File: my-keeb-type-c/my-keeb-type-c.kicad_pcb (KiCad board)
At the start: 2 copper layers, 190.5 x 95.2 mm, 108 parts, among them SW1 SW_Push, U1 ATmega32U4-AU, Y1 16MHz

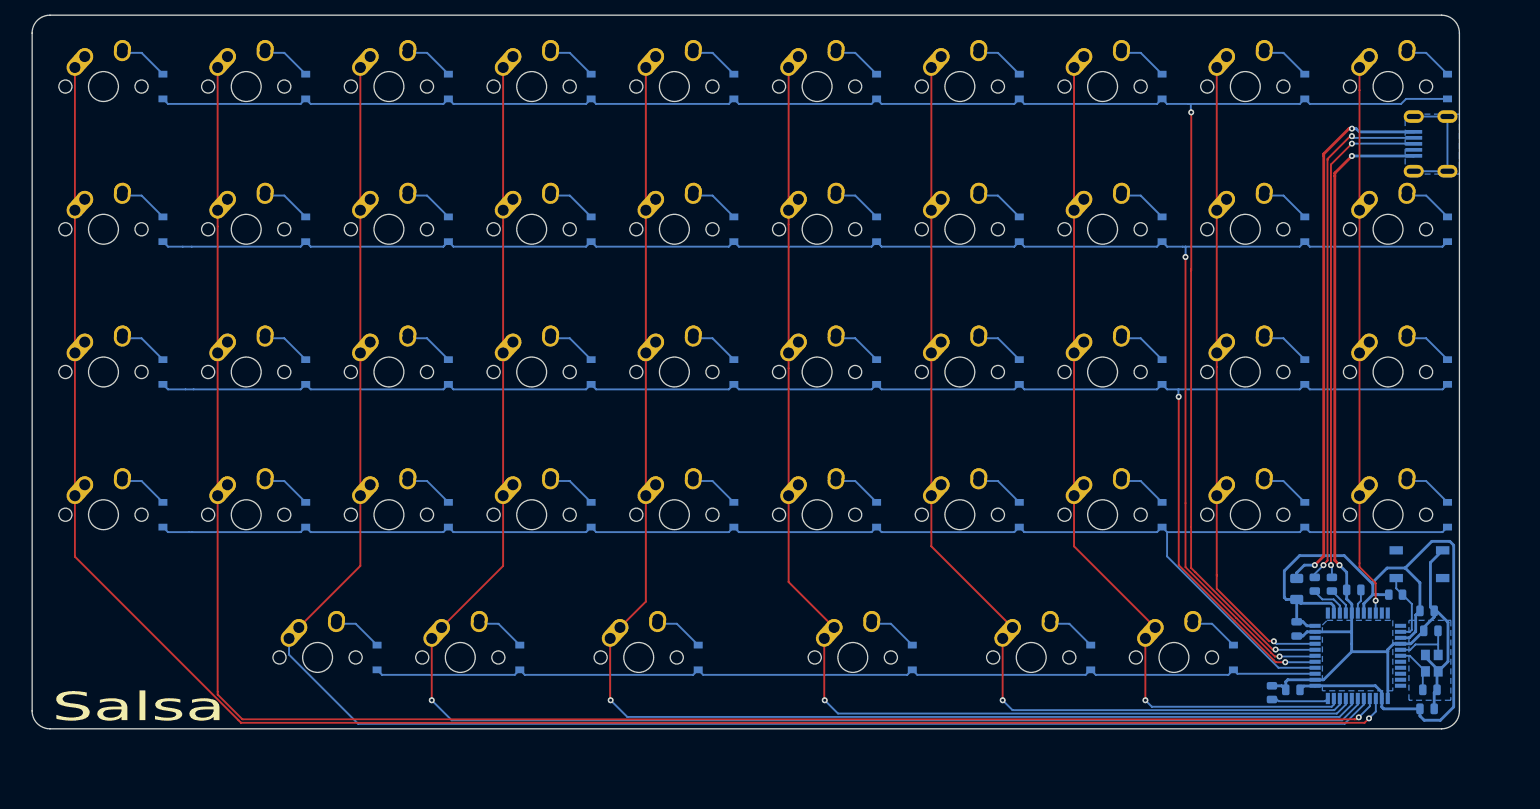
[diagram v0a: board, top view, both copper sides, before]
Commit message: Finished type c model
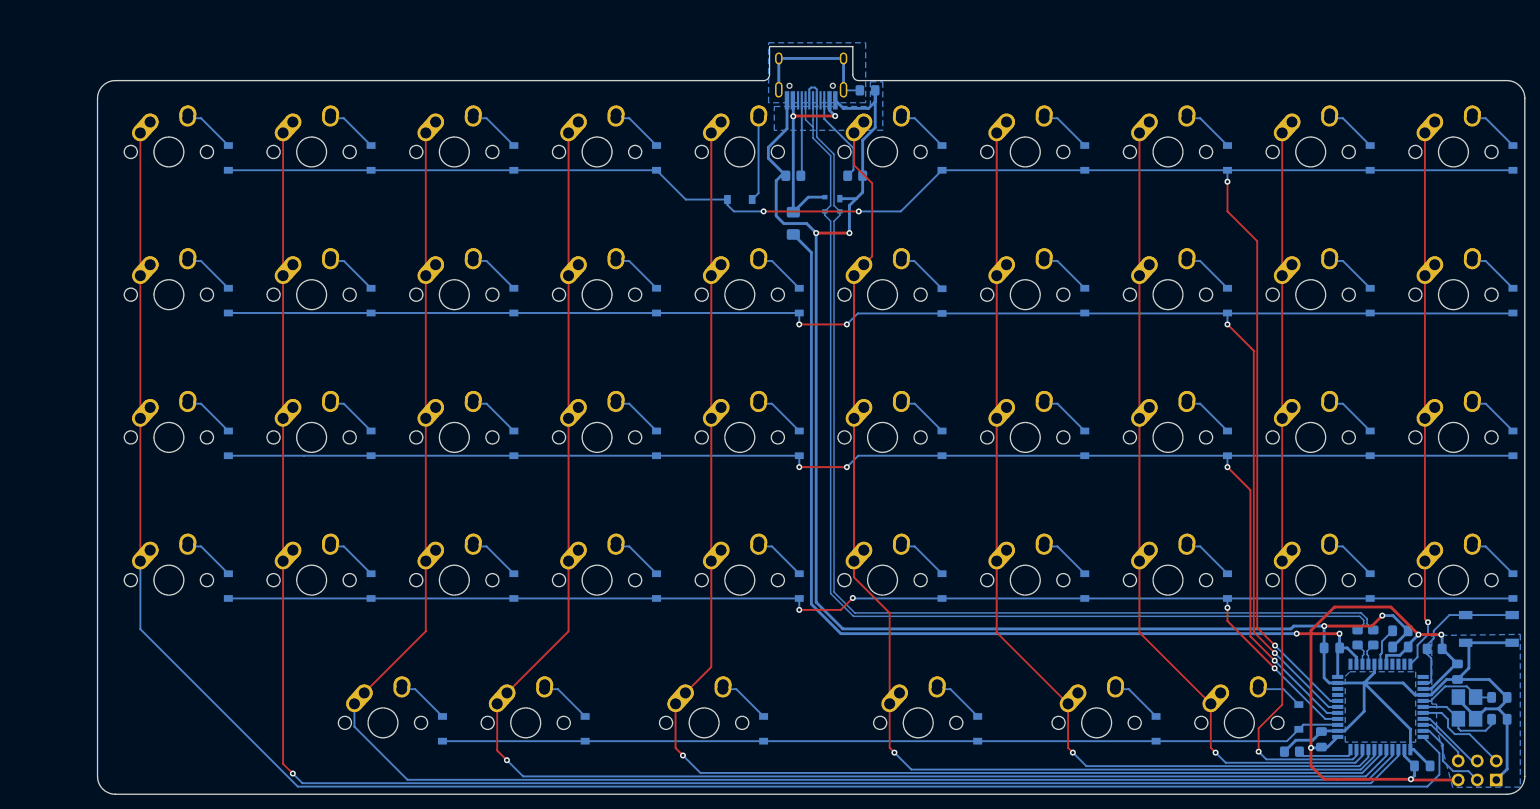
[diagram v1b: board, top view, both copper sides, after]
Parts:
- added C8: 10uF, Capacitor_SMD:C_0805_2012Metric_Pad1.18x1.45mm_HandSolder, B.Cu at (186.2, 97.2)
- added FB1: 60@100MHz, Inductor_SMD:L_0805_2012Metric_Pad1.15x1.40mm_HandSolder, B.Cu at (124.2, 22.7)
- added G***: LOGO, sasha:B.SilkS_layer1, F.Cu at (47.9, 71.0)
- added J1: AVR-ISP-6, random-keyboard-parts:Reset_Pretty-Mask, B.Cu at (205.6, 113.5)
- added R5: 22, Resistor_SMD:R_0805_2012Metric_Pad1.20x1.40mm_HandSolder, B.Cu at (189.6, 95.8)
- added R6: 22, Resistor_SMD:R_0805_2012Metric_Pad1.20x1.40mm_HandSolder, B.Cu at (191.7, 95.8)
- added U2: PRTR5V0U2X, random-keyboard-parts:SOT143B, B.Cu at (119.5, 37.9)
- C1, C2: value 0.1uF -> 22pF; footprint Capacitor_SMD:C_0805_2012Metric -> Capacitor_SMD:C_0805_2012Metric_Pad1.18x1.45mm_HandSolder
- C3: value 22pF -> 0.1uF; footprint Capacitor_SMD:C_0805_2012Metric -> Capacitor_SMD:C_0805_2012Metric_Pad1.18x1.45mm_HandSolder
- C4: value 22pF -> 1uF; footprint Capacitor_SMD:C_0805_2012Metric -> Capacitor_SMD:C_0805_2012Metric_Pad1.18x1.45mm_HandSolder
- C5: footprint Capacitor_SMD:C_0805_2012Metric -> Capacitor_SMD:C_0805_2012Metric_Pad1.18x1.45mm_HandSolder
- C6: value 1uF -> 0.1uF; footprint Capacitor_SMD:C_0805_2012Metric -> Capacitor_SMD:C_0805_2012Metric_Pad1.18x1.45mm_HandSolder
- C7: value 10uF -> 0.1uF; footprint Capacitor_SMD:C_0805_2012Metric -> Capacitor_SMD:C_0805_2012Metric_Pad1.18x1.45mm_HandSolder
- F1: footprint Fuse:Fuse_1206_3216Metric -> Fuse:Fuse_1206_3216Metric_Pad1.42x1.75mm_HandSolder
- R1, R2: value 22 -> 10k; footprint Resistor_SMD:R_0805_2012Metric -> Resistor_SMD:R_0805_2012Metric_Pad1.20x1.40mm_HandSolder
- R3, R4: value 10k -> 5.1k; footprint Resistor_SMD:R_0805_2012Metric -> Resistor_SMD:R_0805_2012Metric_Pad1.20x1.40mm_HandSolder
- SW1: footprint random-keyboard-parts:SKQG-1155865 -> Button_Switch_SMD:SW_SPST_SKQG_WithStem
- USB1: value Molex-0548190589 -> HRO-TYPE-C-31-M-12; footprint random-keyboard-parts:Molex-0548190589 -> Type-C:HRO-TYPE-C-31-M-12-HandSoldering
- Y1: footprint Crystal:Crystal_SMD_3225-4Pin_3.2x2.5mm -> Crystal:Crystal_SMD_3225-4Pin_3.2x2.5mm_HandSoldering
- moved R4 94.0 mm to (114.3, 34.1), turned to 180 degrees
- moved R3 91.3 mm to (122.6, 34.1)
- moved USB1 86.1 mm to (116.7, 15.9), turned to 0 degrees
- moved F1 83.0 mm to (114.3, 40.5)
- moved C2 27.6 mm to (208.5, 103.8), turned to 0 degrees
- moved R2 23.0 mm to (180.8, 111.0), turned to 0 degrees
- moved R1 18.2 mm to (199.9, 97.3), turned to 180 degrees
- moved C6 17.6 mm to (202.9, 100.3), turned to 270 degrees
- moved D19 15.1 mm to (107.2, 37.3), turned to 0 degrees
- moved C7 15.1 mm to (184.8, 109.3), turned to 90 degrees
- moved D25 13.0 mm to (134.1, 50.9)
- moved D27 12.9 mm to (134.1, 88.9)
- moved D37 12.9 mm to (172.2, 88.9)
- moved D24 12.9 mm to (134.1, 31.8)
- moved D34 12.9 mm to (172.2, 31.8)
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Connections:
- C1 pad 1: +5V -> Net-(C1-Pad1)
- C2 pad 1: +5V -> Net-(C2-Pad1)
- C3 pad 1: Net-(C3-Pad1) -> +5V
- C6 pad 1: Net-(C6-Pad1) -> +5V
- R1 pad 1: Net-(R1-Pad1) -> +5V
- R1 pad 2: D- -> Net-(R1-Pad2)
- R2 pad 1: Net-(R2-Pad1) -> GND
- R2 pad 2: D+ -> Net-(R2-Pad2)
- R3 pad 1: +5V -> Net-(R3-Pad1)
- R3 pad 2: Net-(R3-Pad2) -> GND
- R4 pad 1: GND -> Net-(R4-Pad1)
- R4 pad 2: Net-(R4-Pad2) -> GND
- SW1 pad 2: Net-(R3-Pad2) -> Net-(R1-Pad2)
- U1 pad 11: Net-(U1-Pad11) -> COL9
- U1 pad 13: Net-(R3-Pad2) -> Net-(R1-Pad2)
- U1 pad 16: Net-(C4-Pad1) -> Net-(C2-Pad1)
- U1 pad 17: Net-(C3-Pad1) -> Net-(C1-Pad1)
- U1 pad 18: Net-(U1-Pad18) -> RST
- U1 pad 19: Net-(U1-Pad19) -> SCK
- U1 pad 20: Net-(U1-Pad20) -> MISO
- U1 pad 21: Net-(U1-Pad21) -> MOSI
- U1 pad 22: Net-(U1-Pad22) -> COL0
- U1 pad 25: COL0 -> COL1
- U1 pad 26: COL1 -> COL2
- U1 pad 27: COL2 -> COL3
- U1 pad 28: COL3 -> COL4
- U1 pad 29: COL4 -> COL5
- U1 pad 3: Net-(R1-Pad1) -> D-
- U1 pad 30: COL5 -> COL6
- U1 pad 31: COL6 -> COL7
- U1 pad 32: COL7 -> COL8
- U1 pad 33: Net-(R4-Pad2) -> Net-(R2-Pad2)
- U1 pad 4: Net-(R2-Pad1) -> D+
- U1 pad 41: COL8 -> Net-(U1-Pad41)
- U1 pad 6: Net-(C6-Pad1) -> Net-(C4-Pad1)
- U1 pad 9: COL9 -> Net-(U1-Pad9)
- USB1 pad 2: Net-(USB1-Pad2) -> VCC
- USB1 pad 3: D+ -> Net-(USB1-Pad3)
- USB1 pad 4: D- -> Net-(R4-Pad1)
- USB1 pad 5: VCC -> DN
- USB1 pad 6: Net-(USB1-Pad6) -> DP
- Y1 pad 1: Net-(C3-Pad1) -> Net-(C1-Pad1)
- Y1 pad 3: Net-(C4-Pad1) -> Net-(C2-Pad1)
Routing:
- net GND: track 144.9 -> 294.6 mm, vias 2 -> 4
- net DP: track 0.00 -> 145.8 mm
- net DN: track 0.00 -> 145.7 mm
- net +5V: track 110.1 -> 217.3 mm, vias 0 -> 6
- net D-: track 69.4 -> 3.00 mm, vias 2 -> 0
- net D+: track 67.4 -> 2.98 mm, vias 2 -> 0
- net VCC: track 72.6 -> 28.0 mm
- net Net-(R1-Pad2): track 0.00 -> 19.8 mm
- net Earth: track 0.00 -> 19.5 mm
- net Net-(USB1-Pad6): track 16.3 -> 0.00 mm
- net RST: track 0.00 -> 13.0 mm
- net COL8: track 85.8 -> 98.4 mm
- net Net-(C1-Pad1): track 0.00 -> 12.3 mm
- net Net-(R3-Pad1): track 0.00 -> 12.0 mm
- net MOSI: track 0.00 -> 11.2 mm
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- added copper zone on B.Cu, net Earth
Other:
- board size 190.5 x 95.2 mm -> 190.5 x 99.8 mm
- board text added: "salsa"
- board text removed: "Salsa"

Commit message: Reverted
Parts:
- removed G***: LOGO, sasha:B.SilkS_layer1

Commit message: Fixed some stuff
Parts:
- added G***: LOGO, sasha:B.SilkS_layer1, F.Cu at (49.7, 71.5)

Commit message: Created some plateless gasket mount pcbs
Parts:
- removed the G*** at (49.7, 71.5)
- added G***: LOGO, sasha-small:B.SilkS_layer1, F.Cu at (38.1, 87.3)
